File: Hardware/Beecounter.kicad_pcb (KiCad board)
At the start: 2 copper layers, 170 parts, among them J1 Conn_01x03, J10 Conn_01x03, J11 Conn_01x03, J12 Conn_01x03, J13 Conn_01x03, J14 Conn_01x03, J15 Conn_02x20_Odd_Even, J2 Conn_01x03, J3 Conn_01x03, J4 Conn_01x03, J5 Conn_01x03, J6 Conn_01x03, J7 Conn_01x03, J8 Conn_01x03, J9 Conn_01x03, U1 LM393, U10 LM393, U11 H2010, U12 LM393, U13 H2010, U14 LM393, U15 H2010, U16 LM393, U17 H2010, U18 LM393, U19 H2010, U2 H2010, U20 LM393, U21 H2010, U22 LM393, U23 H2010, U24 LM393, U25 H2010, U26 LM393, U27 H2010, U28 LM393, U3 H2010, U4 LM393, U5 H2010, U6 LM393, U7 H2010, U8 LM393, U9 H2010

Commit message: Fix issue with entrance 5. Connected light barrier to pin 10 (GPIO16) instead of 9 (GND)
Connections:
- J15 pad 10: unconnected-(J15-Pin_10-Pad10) -> Net-(D12-K)
- J15 pad 9: Net-(D12-K) -> unconnected-(J15-Pin_9-Pad9)

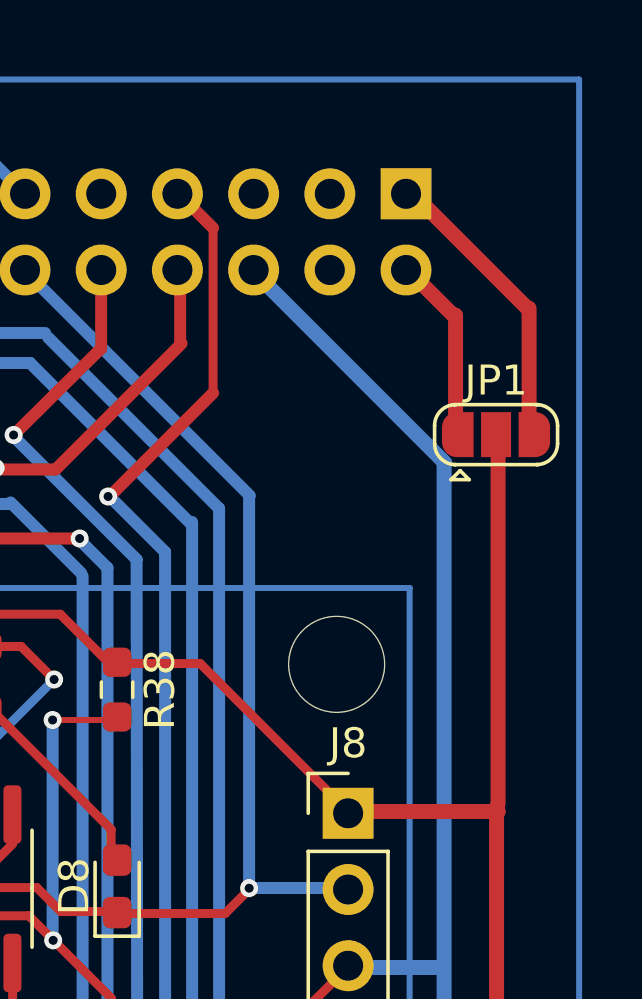
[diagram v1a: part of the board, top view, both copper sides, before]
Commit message: Set power supply for light barriers to 3.3V
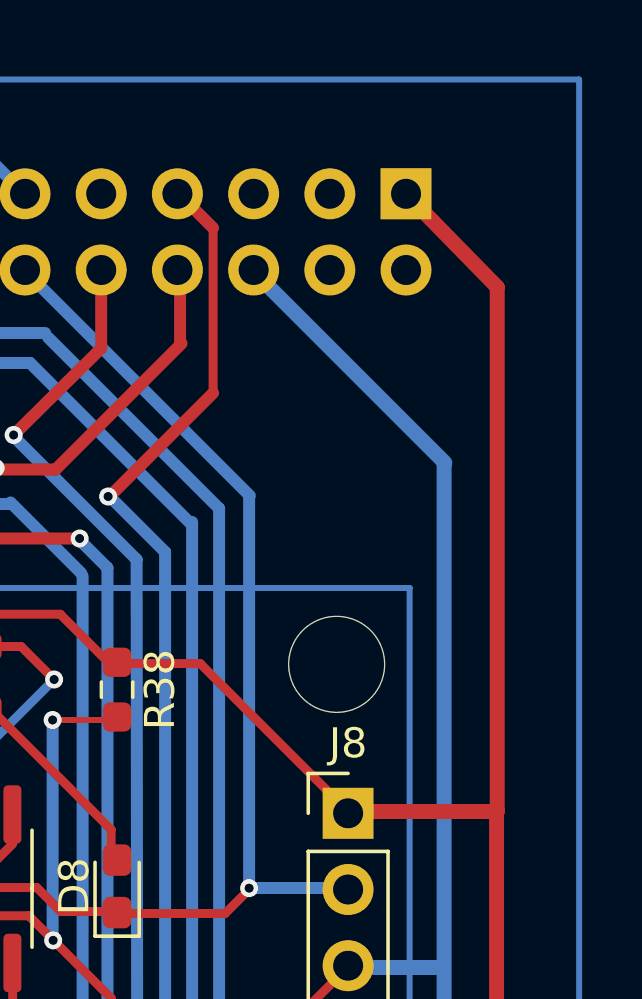
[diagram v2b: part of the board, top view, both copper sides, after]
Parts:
- removed JP1: Jumper_3_Bridged12, Jumper:SolderJumper-3_P1.3mm_Open_RoundedPad1.0x1.5mm
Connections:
- J1 pad 1: +5V -> +3.3V
- J10 pad 1: +5V -> +3.3V
- J11 pad 1: +5V -> +3.3V
- J12 pad 1: +5V -> +3.3V
- J13 pad 1: +5V -> +3.3V
- J14 pad 1: +5V -> +3.3V
- J15 pad 1: Net-(J15-Pin_1) -> +3.3V
- J15 pad 2: Net-(J15-Pin_2) -> unconnected-(J15-Pin_2-Pad2)
- J2 pad 1: +5V -> +3.3V
- J3 pad 1: +5V -> +3.3V
- J4 pad 1: +5V -> +3.3V
- J5 pad 1: +5V -> +3.3V
- J6 pad 1: +5V -> +3.3V
- J7 pad 1: +5V -> +3.3V
- J8 pad 1: +5V -> +3.3V
- J9 pad 1: +5V -> +3.3V
- R1 pad 1: +5V -> +3.3V
- R10 pad 1: +5V -> +3.3V
- R11 pad 1: +5V -> +3.3V
- R12 pad 2: +5V -> +3.3V
- R13 pad 1: +5V -> +3.3V
- R15 pad 1: +5V -> +3.3V
- R16 pad 1: +5V -> +3.3V
- R17 pad 2: +5V -> +3.3V
- R18 pad 1: +5V -> +3.3V
- R2 pad 1: +5V -> +3.3V
- R20 pad 1: +5V -> +3.3V
- R21 pad 1: +5V -> +3.3V
- R22 pad 2: +5V -> +3.3V
- R23 pad 1: +5V -> +3.3V
- R25 pad 1: +5V -> +3.3V
- R26 pad 1: +5V -> +3.3V
- R27 pad 2: +5V -> +3.3V
- R28 pad 1: +5V -> +3.3V
- R30 pad 1: +5V -> +3.3V
- R31 pad 1: +5V -> +3.3V
- R32 pad 2: +5V -> +3.3V
- R33 pad 1: +5V -> +3.3V
- R35 pad 1: +5V -> +3.3V
- R36 pad 1: +5V -> +3.3V
- R37 pad 2: +5V -> +3.3V
- R38 pad 1: +5V -> +3.3V
- R4 pad 2: +5V -> +3.3V
- R40 pad 1: +5V -> +3.3V
- R41 pad 1: +5V -> +3.3V
- R42 pad 2: +5V -> +3.3V
- R43 pad 1: +5V -> +3.3V
- R45 pad 1: +5V -> +3.3V
- R46 pad 1: +5V -> +3.3V
- R47 pad 2: +5V -> +3.3V
- R48 pad 1: +5V -> +3.3V
- R5 pad 1: +5V -> +3.3V
- R50 pad 1: +5V -> +3.3V
- R51 pad 1: +5V -> +3.3V
- R52 pad 2: +5V -> +3.3V
- R53 pad 1: +5V -> +3.3V
- R55 pad 1: +5V -> +3.3V
- R56 pad 1: +5V -> +3.3V
- R57 pad 2: +5V -> +3.3V
- R58 pad 1: +5V -> +3.3V
- R6 pad 1: +5V -> +3.3V
- R60 pad 1: +5V -> +3.3V
- R61 pad 1: +5V -> +3.3V
- R62 pad 2: +5V -> +3.3V
- R63 pad 1: +5V -> +3.3V
- R65 pad 1: +5V -> +3.3V
- R66 pad 1: +5V -> +3.3V
- R67 pad 2: +5V -> +3.3V
- R68 pad 1: +5V -> +3.3V
- R7 pad 2: +5V -> +3.3V
- R70 pad 1: +5V -> +3.3V
- R8 pad 1: +5V -> +3.3V
- U1 pad 5: +5V -> +3.3V
- U1 pad 8: +5V -> +3.3V
- U10 pad 5: +5V -> +3.3V
- U10 pad 8: +5V -> +3.3V
- U12 pad 5: +5V -> +3.3V
- U12 pad 8: +5V -> +3.3V
- U14 pad 5: +5V -> +3.3V
- U14 pad 8: +5V -> +3.3V
- U16 pad 5: +5V -> +3.3V
- U16 pad 8: +5V -> +3.3V
- U18 pad 5: +5V -> +3.3V
- U18 pad 8: +5V -> +3.3V
- U20 pad 5: +5V -> +3.3V
- U20 pad 8: +5V -> +3.3V
- U22 pad 5: +5V -> +3.3V
- U22 pad 8: +5V -> +3.3V
- U24 pad 5: +5V -> +3.3V
- U24 pad 8: +5V -> +3.3V
- U26 pad 5: +5V -> +3.3V
- U26 pad 8: +5V -> +3.3V
- U28 pad 5: +5V -> +3.3V
- U28 pad 8: +5V -> +3.3V
- U4 pad 5: +5V -> +3.3V
- U4 pad 8: +5V -> +3.3V
- U6 pad 5: +5V -> +3.3V
- U6 pad 8: +5V -> +3.3V
- U8 pad 5: +5V -> +3.3V
- U8 pad 8: +5V -> +3.3V
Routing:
- net +5V: track 613.8 -> 0.00 mm, vias 28 -> 0
- net +3.3V: track 0.00 -> 600.7 mm, vias 0 -> 28
- net (no net): track 0.00 -> 13.1 mm

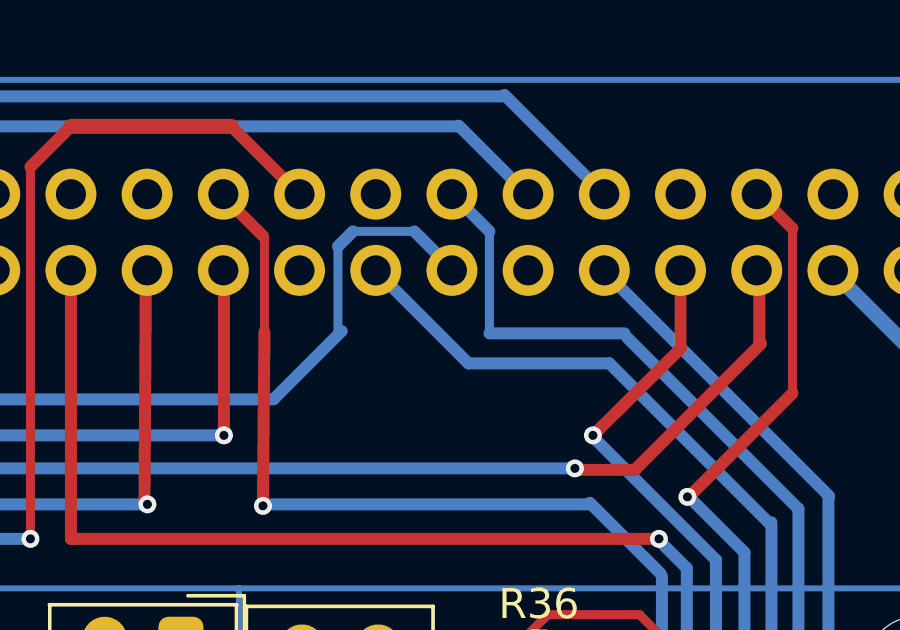
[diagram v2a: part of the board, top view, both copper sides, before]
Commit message: Exchanged pin 16 and 18
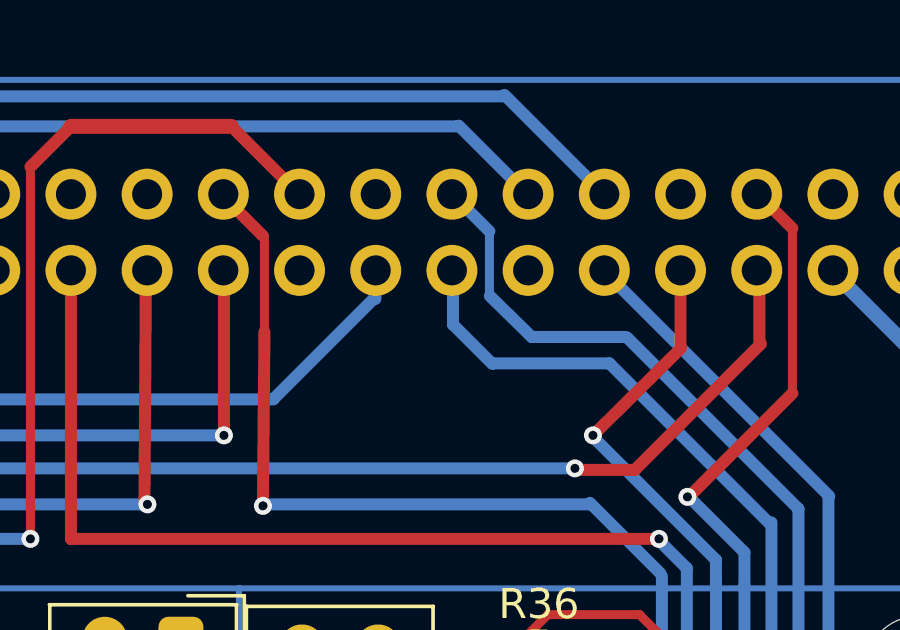
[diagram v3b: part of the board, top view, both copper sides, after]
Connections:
- J15 pad 16: Net-(D3-K) -> Net-(D10-K)
- J15 pad 18: Net-(D10-K) -> Net-(D3-K)
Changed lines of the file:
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@@
 			(layers "*.Cu" "*.Mask")
 			(remove_unused_layers no)
-			(net 18 "Net-(D3-K)")
+			(net 66 "Net-(D10-K)")
 			(pinfunction "Pin_16")
 			(pintype "passive")
@@
 			(layers "*.Cu" "*.Mask")
 			(remove_unused_layers no)
-			(net 66 "Net-(D10-K)")
+			(net 18 "Net-(D3-K)")
 			(pinfunction "Pin_18")
 			(pintype "passive")
@@
 	(gr_line
 		(start 73.35 48.1)
-		(end 73.35 51.5)
+		(end 73.35 50.253657)
 		(stroke
 			(width 0.3)
@@
 	)
 	(gr_line
-		(start 68.3 48.6)
-		(end 68.3 51.427764)
-		(stroke
-			(width 0.3)
-			(type default)
-		)
-		(layer "B.Cu")
-		(net 18)
-	)
-	(gr_line
 		(start 51.825 155.6)
 		(end 51.825 148.199831)
@@
 	)
 	(gr_line
-		(start 69.6 49.45)
-		(end 72.65 52.5)
+		(start 72.135 49.505)
+		(end 72.135 51.205)
 		(stroke
 			(width 0.4)
@@
 	)
 	(gr_line
-		(start 68.425 51.425)
-		(end 66.175 53.675)
+		(start 69.49 50.35)
+		(end 66.169996 53.670004)
 		(stroke
 			(width 0.4)
@@
 	)
 	(gr_line
-		(start 68.8 48.1)
-		(end 68.3 48.6)
-		(stroke
-			(width 0.4)
-			(type default)
-		)
-		(layer "B.Cu")
-		(net 18)
-	)
-	(gr_line
 		(start 84.55 110.05)
 		(end 82.847365 108.347365)
@@
 	)
 	(gr_line
+		(start 69.55 49.44)
+		(end 69.55 50.351976)
+		(stroke
+			(width 0.4)
+			(type default)
+		)
+		(layer "B.Cu")
+		(net 18)
+	)
+	(gr_line
 		(start 88.11192 132.65)
 		(end 91.08808 132.65)
@@
 	)
 	(gr_line
-		(start 72.15 49.4)
-		(end 70.85 48.1)
-		(stroke
-			(width 0.4)
-			(type default)
-		)
-		(layer "B.Cu")
-		(net 18)
-	)
-	(gr_line
-		(start 73.35 51.5)
-		(end 77.851881 51.5)
-		(stroke
-			(width 0.4)
-			(type default)
-		)
-		(layer "B.Cu")
+		(start 74.76 51.62)
+		(end 77.90094 51.62)
+		(stroke
+			(width 0.4)
+			(type default)
+		)
+		(layer "B.Cu")
+		(net 59)
+	)
+	(gr_line
+		(start 73.363614 50.253614)
+		(end 74.76 51.62)
+		(stroke
+			(width 0.4)
+			(type default)
+		)
+		(layer "B.Cu")
+		(net 107)
 	)
 	(gr_rect
@@
 	)
 	(gr_line
-		(start 70.85 48.1)
-		(end 68.8 48.1)
-		(stroke
-			(width 0.3)
-			(type default)
-		)
-		(layer "B.Cu")
-		(net 18)
-	)
-	(gr_line
 		(start 50.4 52.7)
 		(end 46.449684 56.650316)
@@
 	)
 	(gr_line
-		(start 72.65 52.5)
+		(start 73.46 52.5)
 		(end 77.35 52.5)
 		(stroke
 			(width 0.4)
+			(type default)
+		)
+		(layer "B.Cu")
+		(net 66)
+	)
+	(gr_line
+		(start 72.135 51.205)
+		(end 73.445086 52.515086)
+		(stroke
+			(width 0.4)

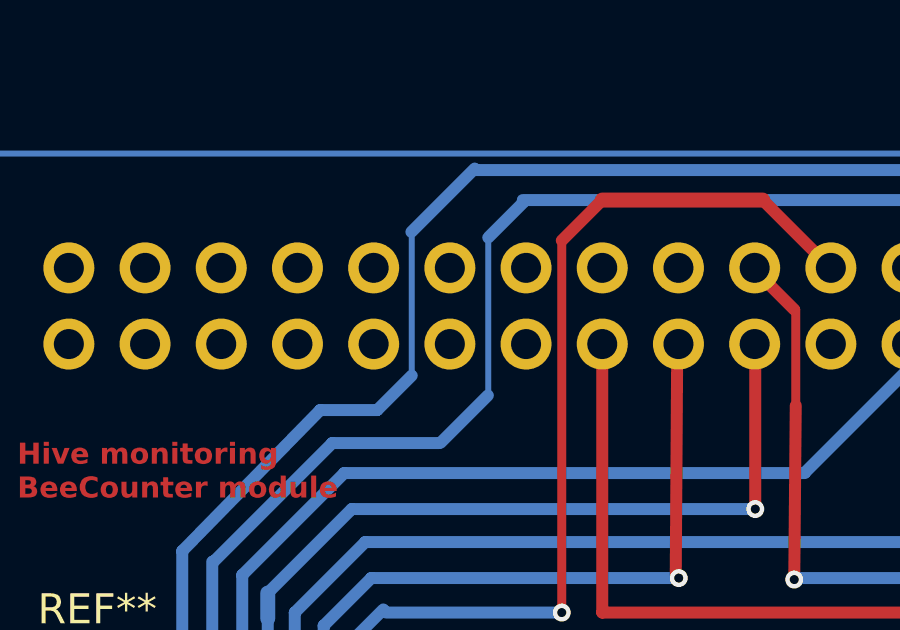
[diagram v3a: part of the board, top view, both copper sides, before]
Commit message: Connected GND pins
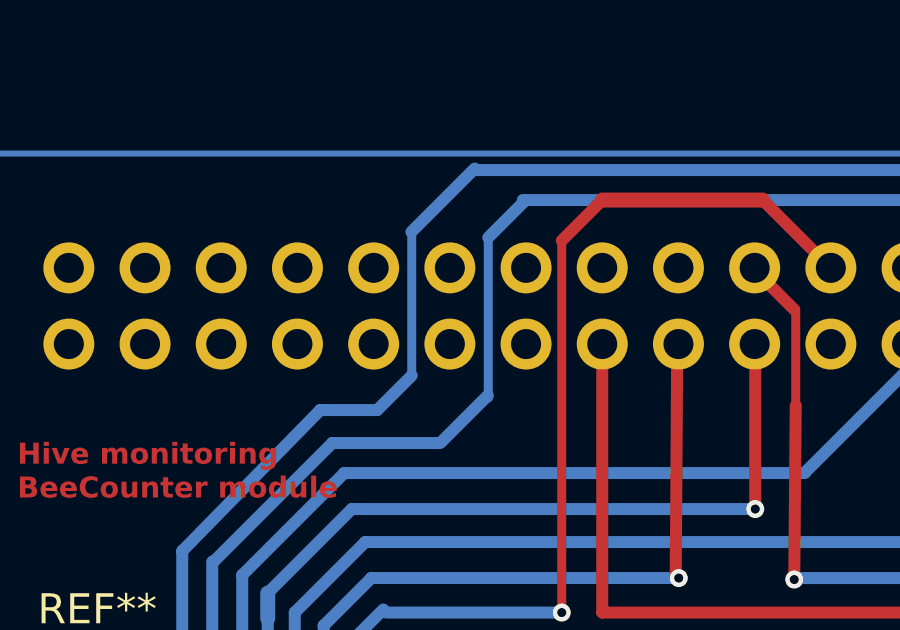
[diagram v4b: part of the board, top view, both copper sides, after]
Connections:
- D3 pad 1: Net-(D3-K) -> Net-(D10-K)
- J15 pad 18: Net-(D3-K) -> Net-(D10-K)
- J15 pad 20: unconnected-(J15-Pin_20-Pad20) -> GND
- J15 pad 25: unconnected-(J15-Pin_25-Pad25) -> GND
- J15 pad 30: unconnected-(J15-Pin_30-Pad30) -> GND
- J15 pad 34: unconnected-(J15-Pin_34-Pad34) -> GND
- J15 pad 39: unconnected-(J15-Pin_39-Pad39) -> GND
- J15 pad 9: unconnected-(J15-Pin_9-Pad9) -> GND
- J3 pad 2: Net-(D3-K) -> Net-(D10-K)
- U6 pad 1: Net-(D3-K) -> Net-(D10-K)
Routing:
- net Net-(D3-K): track 9.06 -> 0.00 mm, vias 1 -> 0
- net (no net): track 13.1 -> 22.2 mm
- net Net-(D10-K): vias 1 -> 2

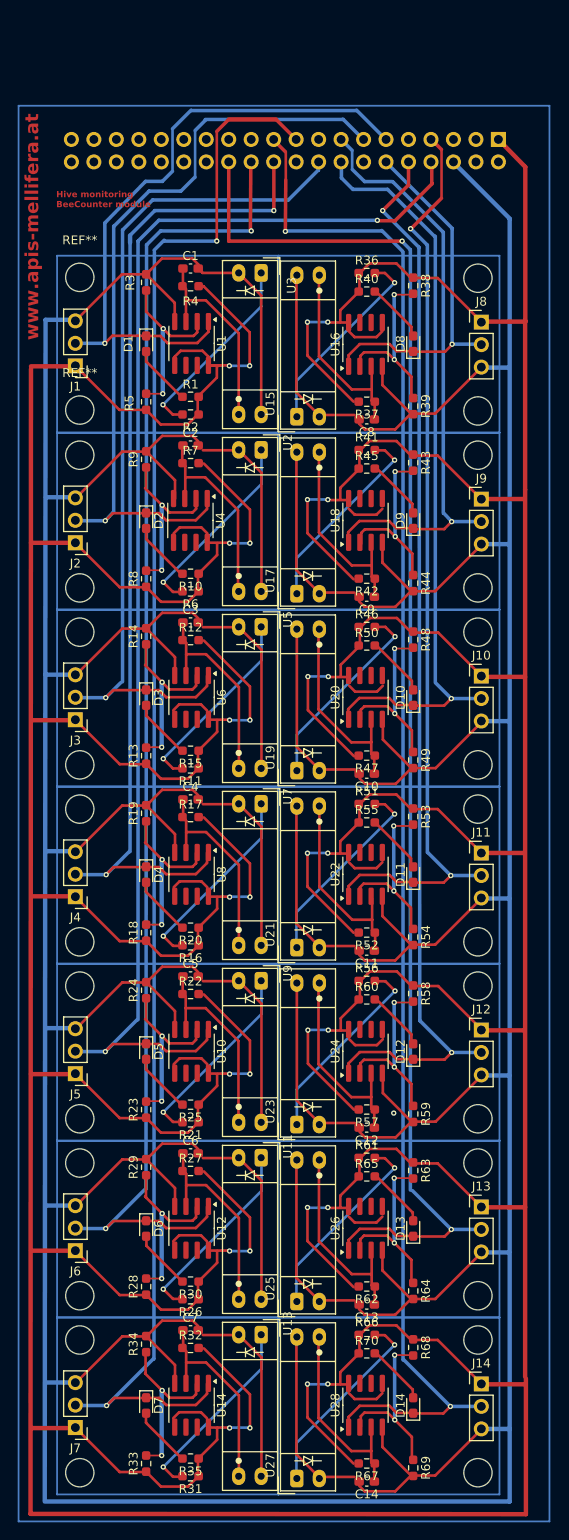
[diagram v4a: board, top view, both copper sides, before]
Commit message: Exchanged pin 13 with 32 and 11 with 36
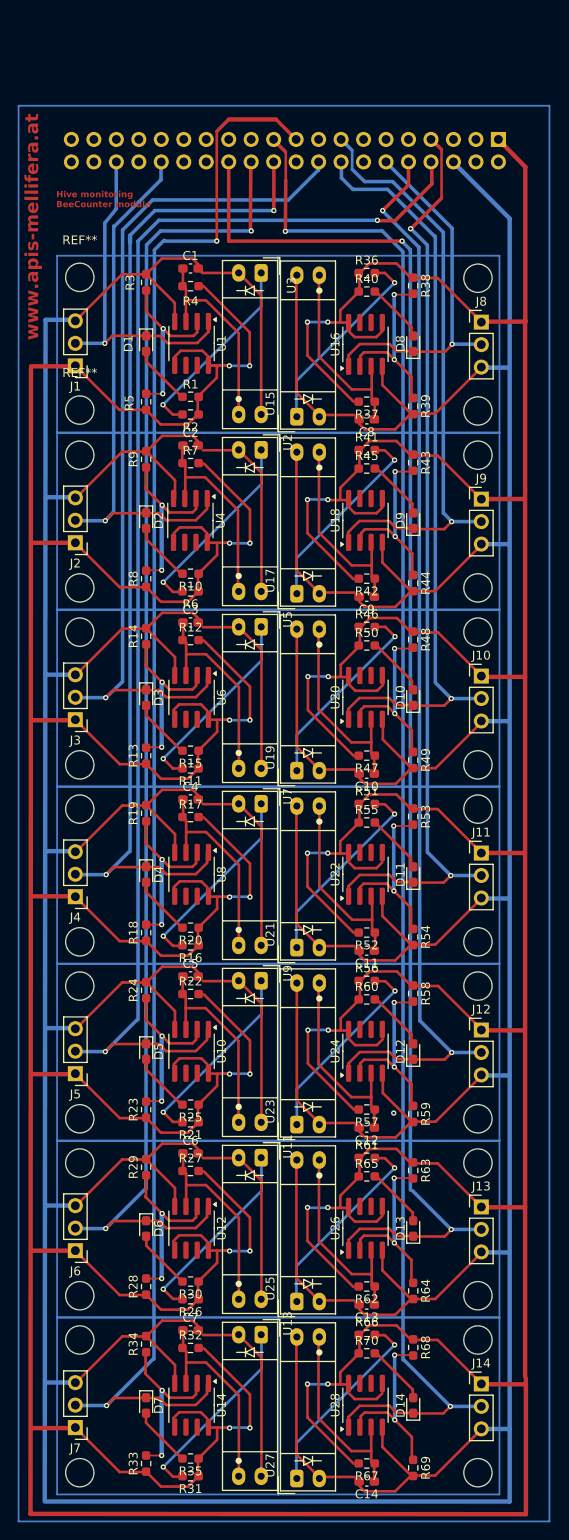
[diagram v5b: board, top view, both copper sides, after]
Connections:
- D3 pad 1: Net-(D10-K) -> Net-(D3-K)
- J15 pad 11: Net-(D1-K) -> unconnected-(J15-Pin_11-Pad11)
- J15 pad 13: Net-(D2-K) -> unconnected-(J15-Pin_13-Pad13)
- J15 pad 18: Net-(D10-K) -> Net-(D3-K)
- J15 pad 32: unconnected-(J15-Pin_32-Pad32) -> Net-(D2-K)
- J15 pad 36: unconnected-(J15-Pin_36-Pad36) -> Net-(D1-K)
- J3 pad 2: Net-(D10-K) -> Net-(D3-K)
- U6 pad 1: Net-(D10-K) -> Net-(D3-K)
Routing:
- net (no net): track 22.2 -> 0.47 mm
- net +3.3V: track 600.7 -> 613.8 mm
- net Net-(D3-K): track 0.00 -> 8.59 mm, vias 0 -> 1
- net Net-(D10-K): vias 2 -> 1

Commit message: Added connector for HX711 (H-bridge) and ADC ADS1115
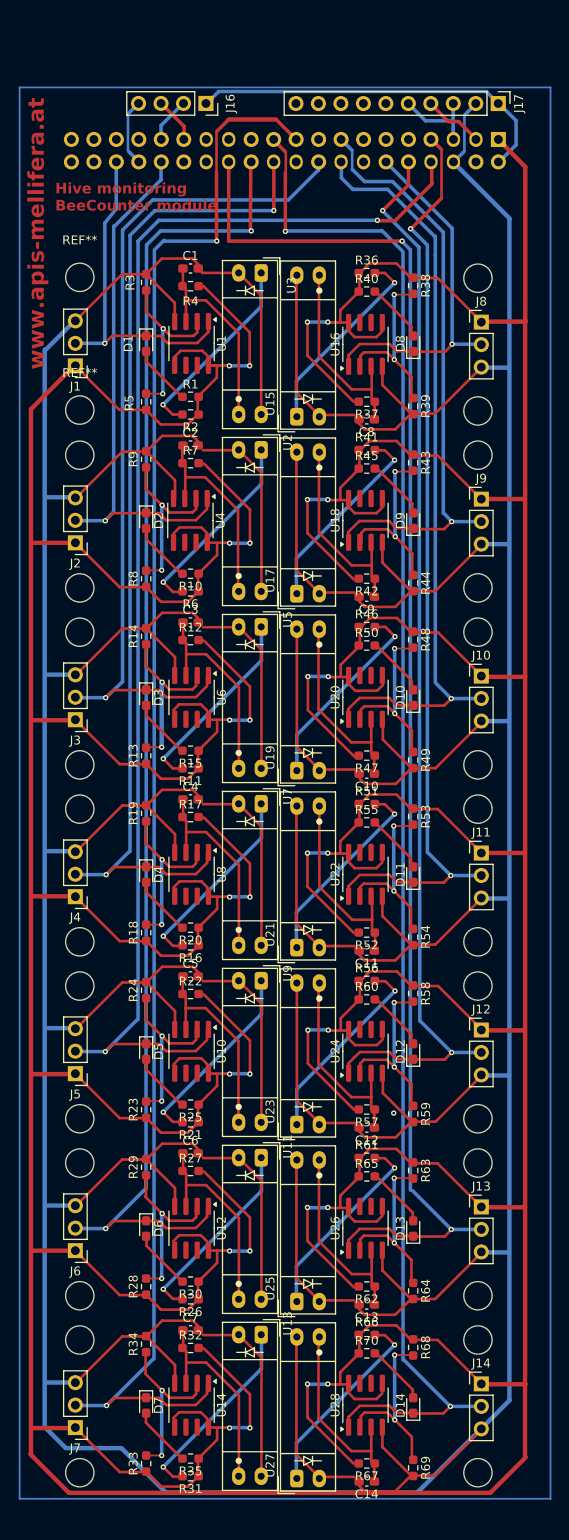
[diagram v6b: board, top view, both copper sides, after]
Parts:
- added J16: Conn_01x04, Connector_PinSocket_2.54mm:PinSocket_1x04_P2.54mm_Vertical, F.Cu at (56.8, 42.8)
- added J17: Conn_01x10, Connector_PinHeader_2.54mm:PinHeader_1x10_P2.54mm_Vertical, F.Cu at (89.9, 42.8)
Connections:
- J15 pad 2: unconnected-(J15-Pin_2-Pad2) -> Net-(J15-Pin_2)
- J15 pad 29: unconnected-(J15-Pin_29-Pad29) -> Net-(J15-Pin_29)
- J15 pad 3: unconnected-(J15-Pin_3-Pad3) -> Net-(J15-Pin_3)
- J15 pad 31: unconnected-(J15-Pin_31-Pad31) -> Net-(J15-Pin_31)
- J15 pad 5: unconnected-(J15-Pin_5-Pad5) -> Net-(J15-Pin_5)
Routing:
- net (no net): track 0.47 -> 0.00 mm, vias 1 -> 0
- net Net-(D12-K): vias 1 -> 2

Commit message: Red layer 0.4mm
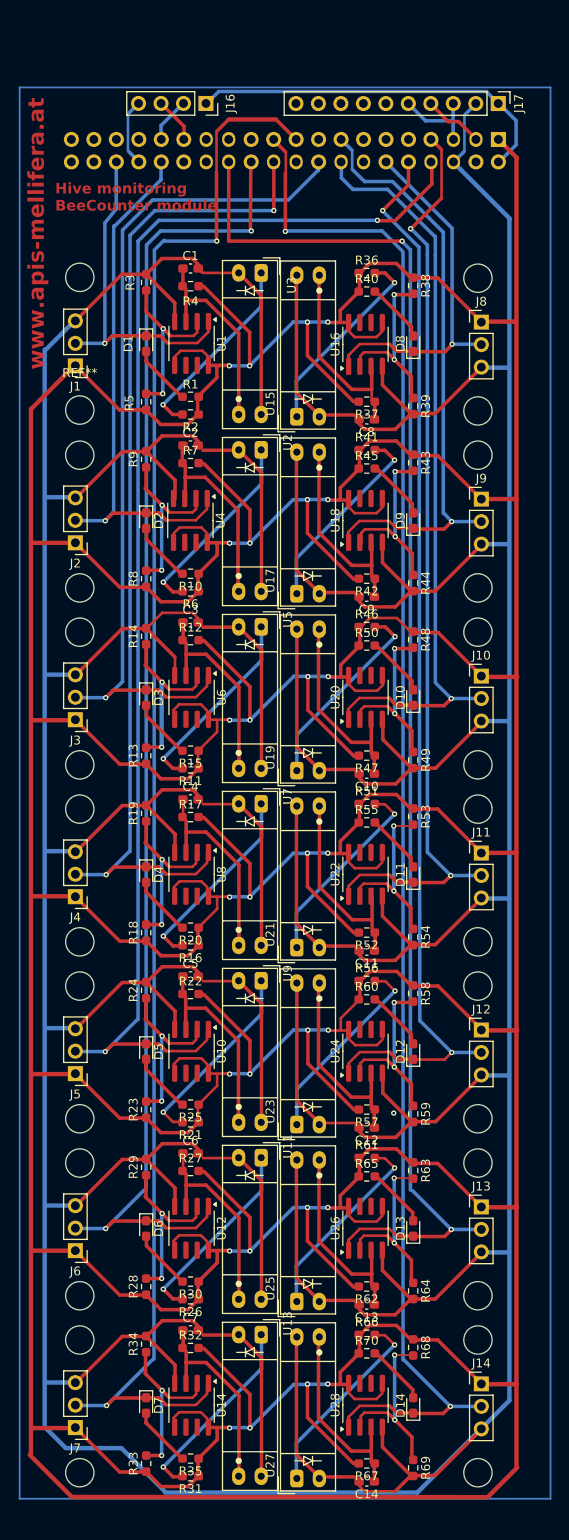
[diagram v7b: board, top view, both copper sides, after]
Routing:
- net +3.3V: track 613.8 -> 673.8 mm
